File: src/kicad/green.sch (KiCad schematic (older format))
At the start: 0 parts

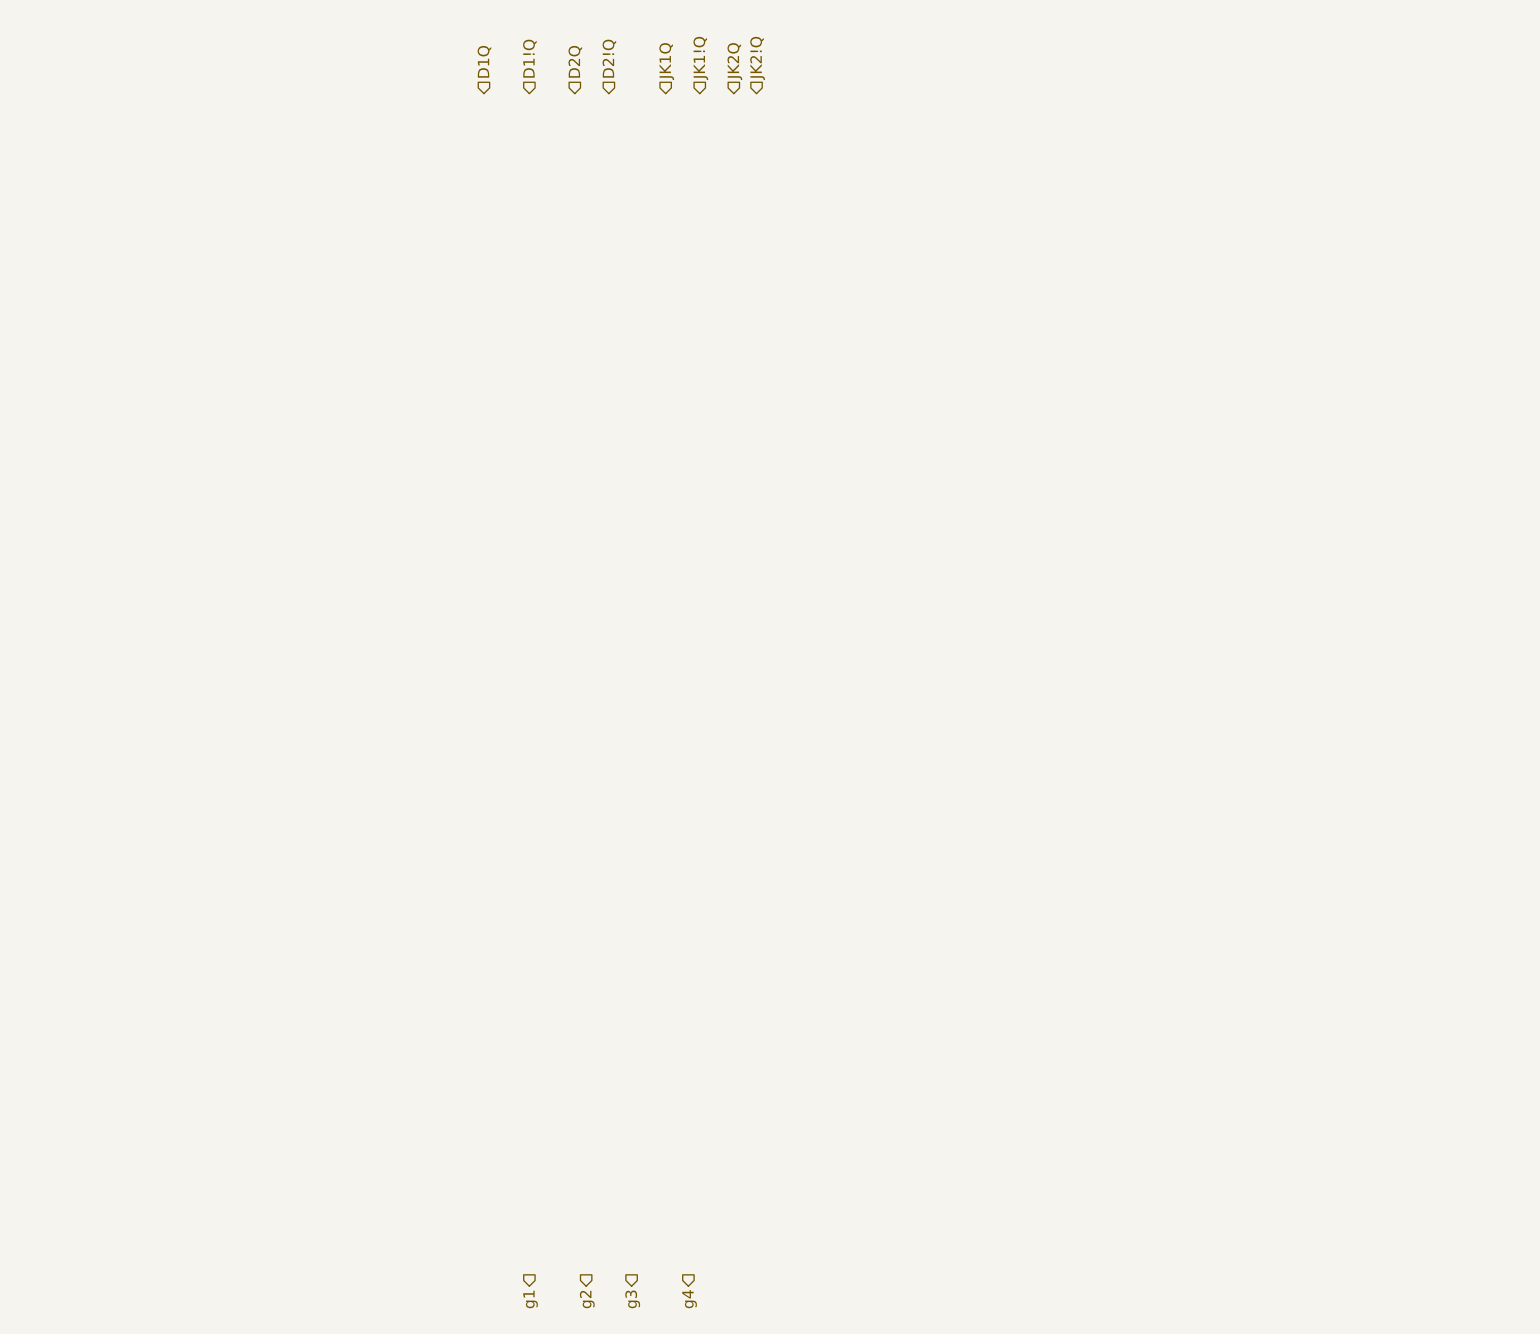
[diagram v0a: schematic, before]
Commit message: finished sub-schemes for LEDs
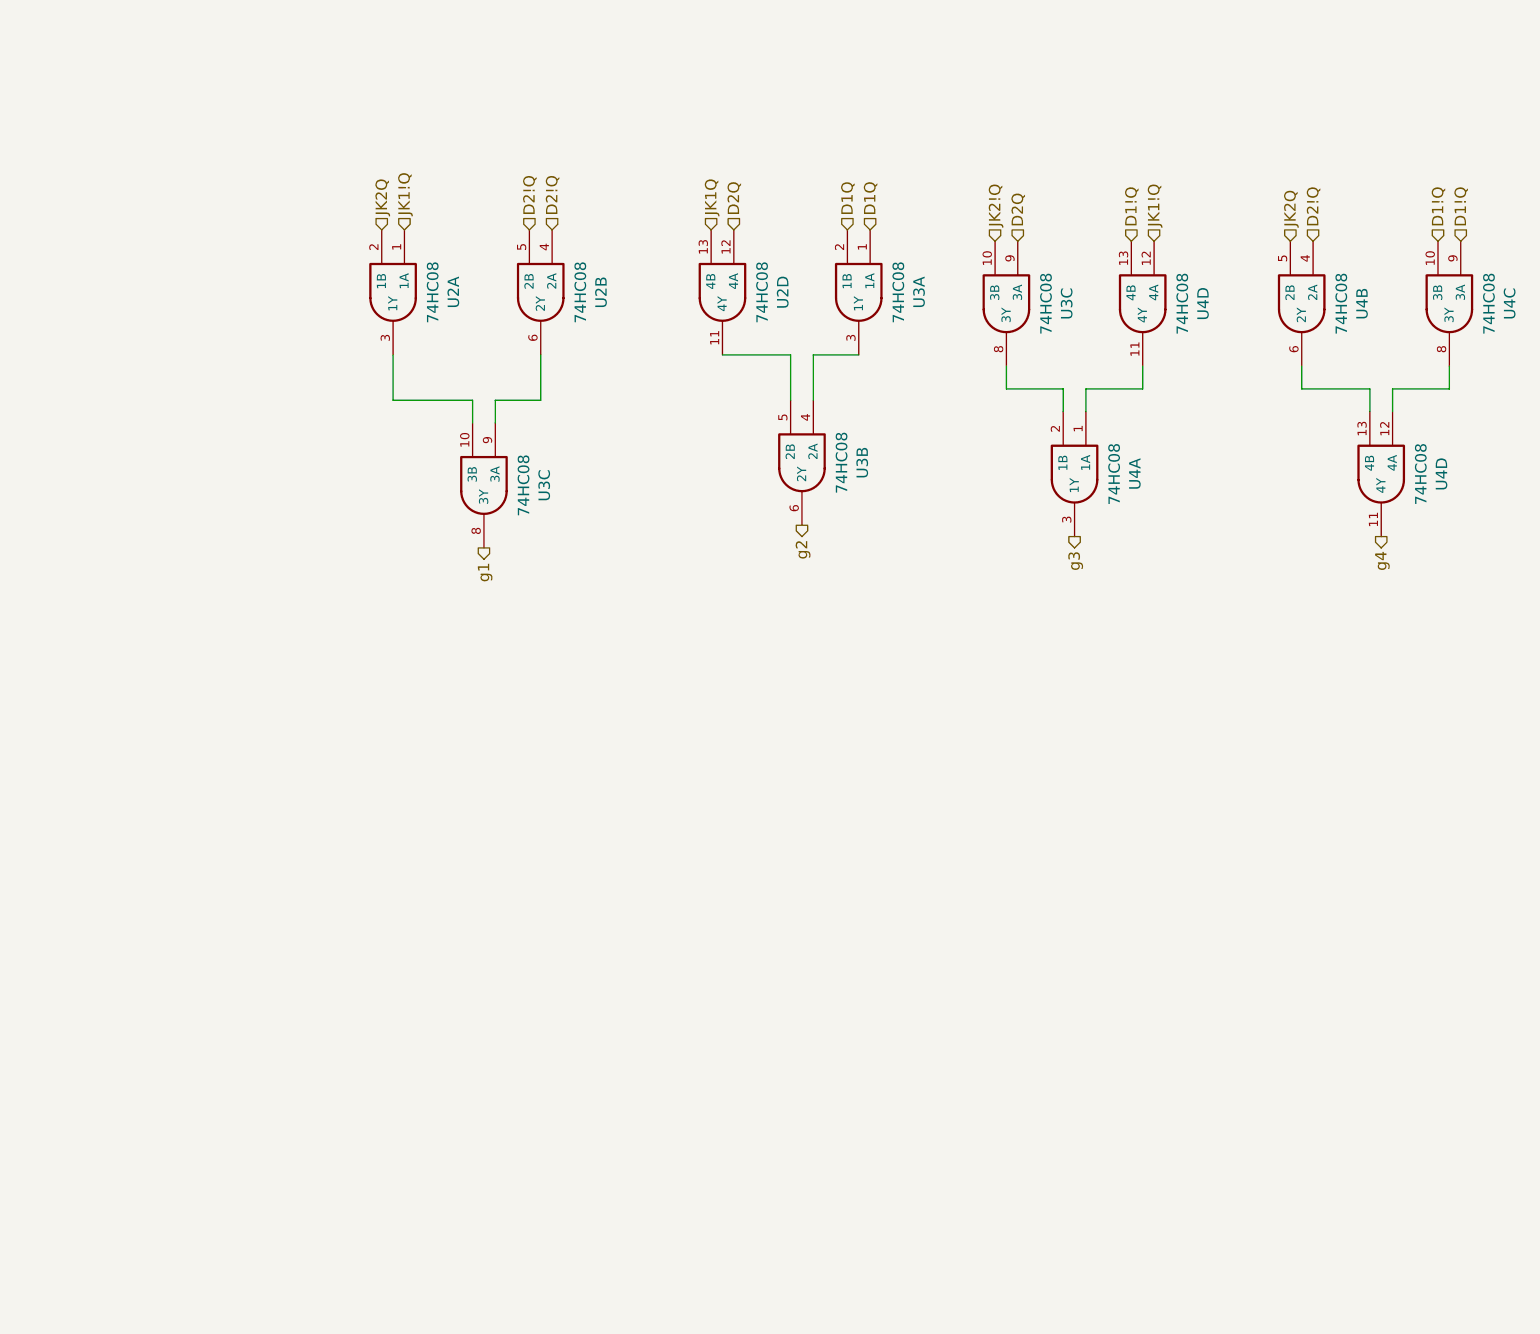
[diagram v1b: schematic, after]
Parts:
- added U2, U3 (x2), U4 (x2): 74HC08, Housings_SOIC:SOIC-14_3.9x8.7mm_Pitch1.27mm, symbol PB170:74HC08
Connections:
- net D1!Q: now also U4.10 (3B), U4.13 (4B), U4.9 (3A)
- net D1Q: now also U3.1 (1A), U3.2 (1B)
- net D2!Q: now also U2.4 (2A), U2.5 (2B), U4.4 (2A)
- net D2Q: now also U2.12 (4A), U3.9 (3A)
- net JK1!Q: now also U2.1 (1A), U4.12 (4A)
- net JK1Q: now also U2.13 (4B)
- net JK2!Q: now also U3.10 (3B)
- net JK2Q: now also U2.2 (1B), U4.5 (2B)
- net g1: now also U3.8 (3Y)
- net g2: now also U3.6 (2Y)
- net g3: now also U4.3 (1Y)
- net g4: now also U4.11 (4Y)
- new net: U2.3 (1Y), U3.10 (3B)
- new net: U2.6 (2Y), U3.9 (3A)
- new net: U2.11 (4Y), U3.5 (2B)
- new net: U3.3 (1Y), U3.4 (2A)
- new net: U3.8 (3Y), U4.2 (1B)
- new net: U4.1 (1A), U4.11 (4Y)
- new net: U4.13 (4B), U4.6 (2Y)
- new net: U4.12 (4A), U4.8 (3Y)

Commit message: fixed annotaion
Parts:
- renumbered U3 to U2, U4 to U3
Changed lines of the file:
@@
 $Descr A4 11693 8268
 encoding utf-8
-Sheet 5 6
+Sheet 4 5
 Title ""
 Date ""
@@
 P 2800 3200
 AR Path="/5FFE1BA5" Ref="U?"  Part="2"
-AR Path="/6006FC3B/5FFE1BA5" Ref="U3"  Part="3"
-F 0 "U3" H 2825 3467 50  0000 C CNN
+AR Path="/6006FC3B/5FFE1BA5" Ref="U2"  Part="3"
+F 0 "U2" H 2825 3467 50  0000 C CNN
 F 1 "74HC08" H 2825 3376 50  0000 C CNN
 F 2 "Housings_SOIC:SOIC-14_3.9x8.7mm_Pitch1.27mm" H 2800 3200 50  0001 C CNN
@@
 P 6750 3150
 AR Path="/5FFEBE04" Ref="U?"  Part="2"
-AR Path="/6006FC3B/5FFEBE04" Ref="U4"  Part="4"
-F 0 "U4" H 6775 3417 50  0000 C CNN
+AR Path="/6006FC3B/5FFEBE04" Ref="U3"  Part="4"
+F 0 "U3" H 6775 3417 50  0000 C CNN
 F 1 "74HC08" H 6775 3326 50  0000 C CNN
 F 2 "Housings_SOIC:SOIC-14_3.9x8.7mm_Pitch1.27mm" H 6750 3150 50  0001 C CNN

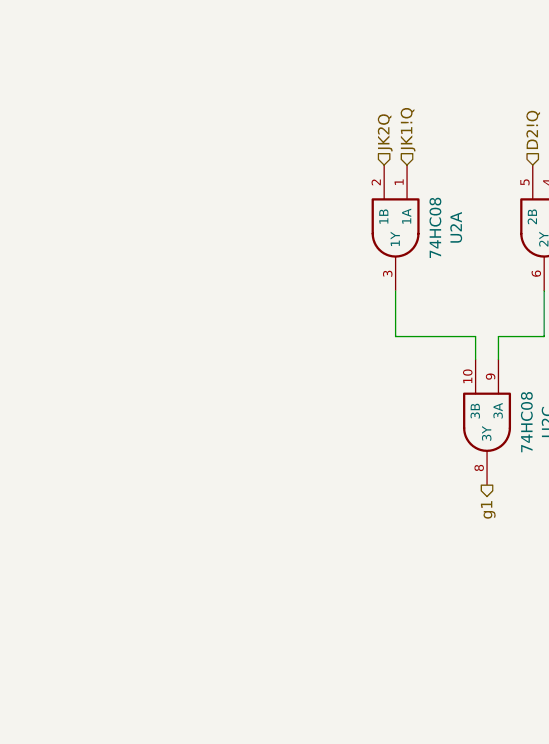
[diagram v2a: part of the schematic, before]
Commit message: added annotations, power connections to parts
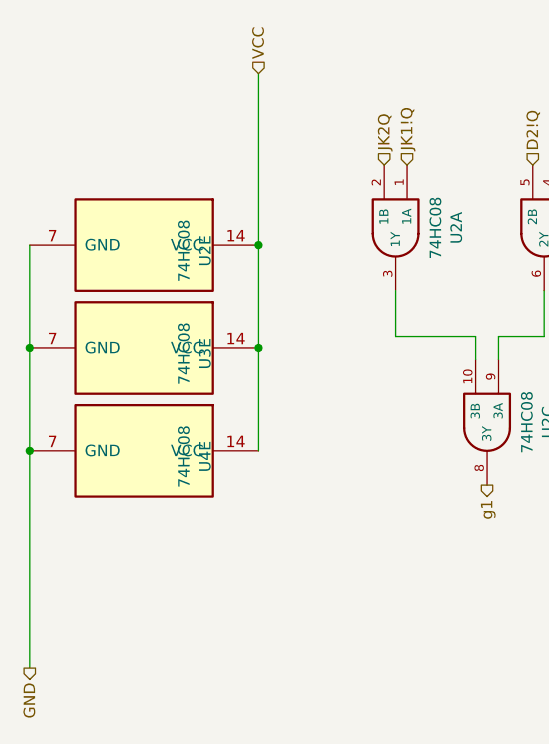
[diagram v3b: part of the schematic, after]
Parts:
- added unit 5 of U2
- added unit 5 of U3
- added unit 5 of U4
- U2, U3, U4: footprint Housings_SOIC:SOIC-14_3.9x8.7mm_Pitch1.27mm -> Package_SO:SOIC-14_3.9x8.7mm_P1.27mm
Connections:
- new net GND: U2.7 (GND), U3.7 (GND), U4.7 (GND)
- new net VCC: U2.14 (VCC), U3.14 (VCC), U4.14 (VCC)
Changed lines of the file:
@@
 F 0 "U2" H 2425 2617 50  0000 C CNN
 F 1 "74HC08" H 2425 2526 50  0000 C CNN
-F 2 "Housings_SOIC:SOIC-14_3.9x8.7mm_Pitch1.27mm" H 2400 2350 50  0001 C CNN
+F 2 "Package_SO:SOIC-14_3.9x8.7mm_P1.27mm" H 2400 2350 50  0001 C CNN
 F 3 "https://datasheet.lcsc.com/szlcsc/Nexperia-74HC08D-653_C5593.pdf" H 2400 2350 50  0001 C CNN
 F 4 "C5593" H 2400 2350 50  0001 C CNN "LCSC"
@@
 F 0 "U2" H 3075 2617 50  0000 C CNN
 F 1 "74HC08" H 3075 2526 50  0000 C CNN
-F 2 "Housings_SOIC:SOIC-14_3.9x8.7mm_Pitch1.27mm" H 3050 2350 50  0001 C CNN
+F 2 "Package_SO:SOIC-14_3.9x8.7mm_P1.27mm" H 3050 2350 50  0001 C CNN
 F 3 "https://datasheet.lcsc.com/szlcsc/Nexperia-74HC08D-653_C5593.pdf" H 3050 2350 50  0001 C CNN
 F 4 "C5593" H 3050 2350 50  0001 C CNN "LCSC"
@@
 F 0 "U2" H 2825 3467 50  0000 C CNN
 F 1 "74HC08" H 2825 3376 50  0000 C CNN
-F 2 "Housings_SOIC:SOIC-14_3.9x8.7mm_Pitch1.27mm" H 2800 3200 50  0001 C CNN
+F 2 "Package_SO:SOIC-14_3.9x8.7mm_P1.27mm" H 2800 3200 50  0001 C CNN
 F 3 "https://datasheet.lcsc.com/szlcsc/Nexperia-74HC08D-653_C5593.pdf" H 2800 3200 50  0001 C CNN
 F 4 "C5593" H 2800 3200 50  0001 C CNN "LCSC"
@@
 F 0 "U2" H 3875 2617 50  0000 C CNN
 F 1 "74HC08" H 3875 2526 50  0000 C CNN
-F 2 "Housings_SOIC:SOIC-14_3.9x8.7mm_Pitch1.27mm" H 3850 2350 50  0001 C CNN
+F 2 "Package_SO:SOIC-14_3.9x8.7mm_P1.27mm" H 3850 2350 50  0001 C CNN
 F 3 "https://datasheet.lcsc.com/szlcsc/Nexperia-74HC08D-653_C5593.pdf" H 3850 2350 50  0001 C CNN
 F 4 "C5593" H 3850 2350 50  0001 C CNN "LCSC"
@@
 F 0 "U3" H 4475 2617 50  0000 C CNN
 F 1 "74HC08" H 4475 2526 50  0000 C CNN
-F 2 "Housings_SOIC:SOIC-14_3.9x8.7mm_Pitch1.27mm" H 4450 2350 50  0001 C CNN
+F 2 "Package_SO:SOIC-14_3.9x8.7mm_P1.27mm" H 4450 2350 50  0001 C CNN
 F 3 "https://datasheet.lcsc.com/szlcsc/Nexperia-74HC08D-653_C5593.pdf" H 4450 2350 50  0001 C CNN
 F 4 "C5593" H 4450 2350 50  0001 C CNN "LCSC"
@@
 F 0 "U3" H 4225 3367 50  0000 C CNN
 F 1 "74HC08" H 4225 3276 50  0000 C CNN
-F 2 "Housings_SOIC:SOIC-14_3.9x8.7mm_Pitch1.27mm" H 4200 3100 50  0001 C CNN
+F 2 "Package_SO:SOIC-14_3.9x8.7mm_P1.27mm" H 4200 3100 50  0001 C CNN
 F 3 "https://datasheet.lcsc.com/szlcsc/Nexperia-74HC08D-653_C5593.pdf" H 4200 3100 50  0001 C CNN
 F 4 "C5593" H 4200 3100 50  0001 C CNN "LCSC"
@@
 F 0 "U3" H 5125 2667 50  0000 C CNN
 F 1 "74HC08" H 5125 2576 50  0000 C CNN
-F 2 "Housings_SOIC:SOIC-14_3.9x8.7mm_Pitch1.27mm" H 5100 2400 50  0001 C CNN
+F 2 "Package_SO:SOIC-14_3.9x8.7mm_P1.27mm" H 5100 2400 50  0001 C CNN
 F 3 "https://datasheet.lcsc.com/szlcsc/Nexperia-74HC08D-653_C5593.pdf" H 5100 2400 50  0001 C CNN
 F 4 "C5593" H 5100 2400 50  0001 C CNN "LCSC"
@@
 F 0 "U4" H 5725 2667 50  0000 C CNN
 F 1 "74HC08" H 5725 2576 50  0000 C CNN
-F 2 "Housings_SOIC:SOIC-14_3.9x8.7mm_Pitch1.27mm" H 5700 2400 50  0001 C CNN
+F 2 "Package_SO:SOIC-14_3.9x8.7mm_P1.27mm" H 5700 2400 50  0001 C CNN
 F 3 "https://datasheet.lcsc.com/szlcsc/Nexperia-74HC08D-653_C5593.pdf" H 5700 2400 50  0001 C CNN
 F 4 "C5593" H 5700 2400 50  0001 C CNN "LCSC"
@@
 F 0 "U4" H 5425 3417 50  0000 C CNN
 F 1 "74HC08" H 5425 3326 50  0000 C CNN
-F 2 "Housings_SOIC:SOIC-14_3.9x8.7mm_Pitch1.27mm" H 5400 3150 50  0001 C CNN
+F 2 "Package_SO:SOIC-14_3.9x8.7mm_P1.27mm" H 5400 3150 50  0001 C CNN
 F 3 "https://datasheet.lcsc.com/szlcsc/Nexperia-74HC08D-653_C5593.pdf" H 5400 3150 50  0001 C CNN
 F 4 "C5593" H 5400 3150 50  0001 C CNN "LCSC"
@@
 F 0 "U4" H 6425 2667 50  0000 C CNN
 F 1 "74HC08" H 6425 2576 50  0000 C CNN
-F 2 "Housings_SOIC:SOIC-14_3.9x8.7mm_Pitch1.27mm" H 6400 2400 50  0001 C CNN
+F 2 "Package_SO:SOIC-14_3.9x8.7mm_P1.27mm" H 6400 2400 50  0001 C CNN
 F 3 "https://datasheet.lcsc.com/szlcsc/Nexperia-74HC08D-653_C5593.pdf" H 6400 2400 50  0001 C CNN
 F 4 "C5593" H 6400 2400 50  0001 C CNN "LCSC"
@@
 F 0 "U4" H 7075 2667 50  0000 C CNN
 F 1 "74HC08" H 7075 2576 50  0000 C CNN
-F 2 "Housings_SOIC:SOIC-14_3.9x8.7mm_Pitch1.27mm" H 7050 2400 50  0001 C CNN
+F 2 "Package_SO:SOIC-14_3.9x8.7mm_P1.27mm" H 7050 2400 50  0001 C CNN
 F 3 "https://datasheet.lcsc.com/szlcsc/Nexperia-74HC08D-653_C5593.pdf" H 7050 2400 50  0001 C CNN
 F 4 "C5593" H 7050 2400 50  0001 C CNN "LCSC"
@@
 F 0 "U3" H 6775 3417 50  0000 C CNN
 F 1 "74HC08" H 6775 3326 50  0000 C CNN
-F 2 "Housings_SOIC:SOIC-14_3.9x8.7mm_Pitch1.27mm" H 6750 3150 50  0001 C CNN
+F 2 "Package_SO:SOIC-14_3.9x8.7mm_P1.27mm" H 6750 3150 50  0001 C CNN
 F 3 "https://datasheet.lcsc.com/szlcsc/Nexperia-74HC08D-653_C5593.pdf" H 6750 3150 50  0001 C CNN
 F 4 "C5593" H 6750 3150 50  0001 C CNN "LCSC"
@@
 Text HLabel 7100 2150 1    50   Input ~ 0
 D1!Q
+$Comp
+L PB170:74HC08 U?
+U 5 1 606691F5
+P 1300 2450
+AR Path="/606691F5" Ref="U?"  Part="2"
+AR Path="/6006FC3B/606691F5" Ref="U2"  Part="5"
+AR Path="/6004480C/606691F5" Ref="U?"  Part="5"
+F 0 "U2" H 1325 2717 50  0000 C CNN
+F 1 "74HC08" H 1325 2626 50  0000 C CNN
+F 2 "Package_SO:SOIC-14_3.9x8.7mm_P1.27mm" H 1300 2450 50  0001 C CNN
+F 3 "https://datasheet.lcsc.com/szlcsc/Nexperia-74HC08D-653_C5593.pdf" H 1300 2450 50  0001 C CNN
+F 4 "C5593" H 1300 2450 50  0001 C CNN "LCSC"
+	5    1300 2450
+	0    1    1    0
+$EndComp
+$Comp
+L PB170:74HC08 U?
+U 5 1 606698AA
+P 1300 2900
+AR Path="/606698AA" Ref="U?"  Part="2"
+AR Path="/6006FC3B/606698AA" Ref="U3"  Part="5"
+AR Path="/6004480C/606698AA" Ref="U?"  Part="5"
+F 0 "U3" H 1325 3167 50  0000 C CNN
+F 1 "74HC08" H 1325 3076 50  0000 C CNN
+F 2 "Package_SO:SOIC-14_3.9x8.7mm_P1.27mm" H 1300 2900 50  0001 C CNN
+F 3 "https://datasheet.lcsc.com/szlcsc/Nexperia-74HC08D-653_C5593.pdf" H 1300 2900 50  0001 C CNN
+F 4 "C5593" H 1300 2900 50  0001 C CNN "LCSC"
+	5    1300 2900
+	0    1    1    0
+$EndComp
+$Comp
+L PB170:74HC08 U?
+U 5 1 60669DC5
+P 1300 3350
+AR Path="/60669DC5" Ref="U?"  Part="2"
+AR Path="/6006FC3B/60669DC5" Ref="U4"  Part="5"
+AR Path="/6004480C/60669DC5" Ref="U?"  Part="5"
+F 0 "U4" H 1325 3617 50  0000 C CNN
+F 1 "74HC08" H 1325 3526 50  0000 C CNN
+F 2 "Package_SO:SOIC-14_3.9x8.7mm_P1.27mm" H 1300 3350 50  0001 C CNN
+F 3 "https://datasheet.lcsc.com/szlcsc/Nexperia-74HC08D-653_C5593.pdf" H 1300 3350 50  0001 C CNN
+F 4 "C5593" H 1300 3350 50  0001 C CNN "LCSC"
+	5    1300 3350
+	0    1    1    0
+$EndComp
+Wire Wire Line
+	800  2900 800  2450
+Wire Wire Line
+	800  2900 800  3350
+Connection ~ 800  2900
+Connection ~ 800  3350
+Wire Wire Line
+	800  3350 800  4300
+Wire Wire Line
+	1800 3350 1800 2900
+Wire Wire Line
+	1800 2900 1800 2450
+Connection ~ 1800 2900
+Wire Wire Line
+	1800 2450 1800 1700
+Connection ~ 1800 2450
+Text HLabel 1800 1700 1    50   Input ~ 0
+VCC
+Text HLabel 800  4300 3    50   Output ~ 0
+GND
 $EndSCHEMATC

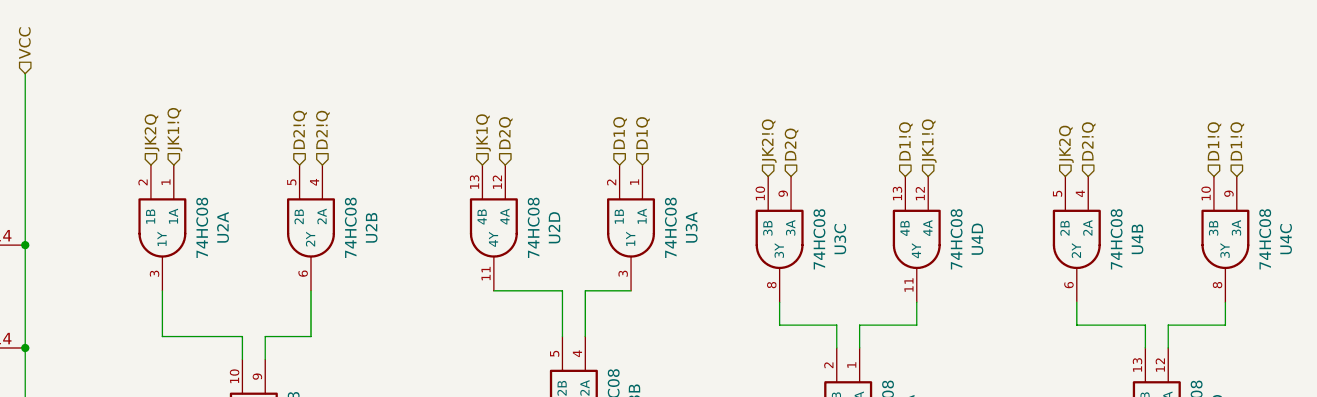
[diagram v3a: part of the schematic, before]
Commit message: Corrected negations
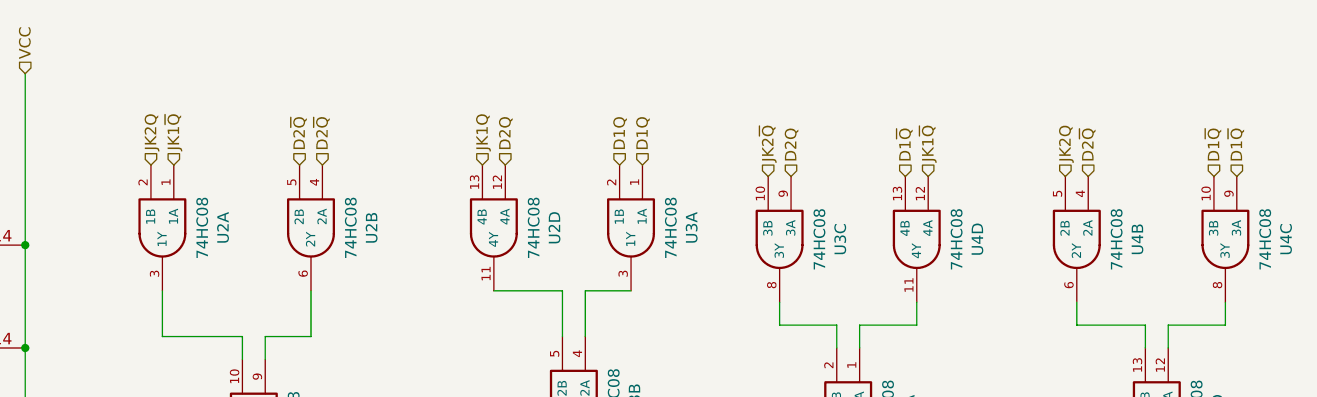
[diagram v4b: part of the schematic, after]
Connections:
- net D1!Q renamed D1~Q
- net D2!Q renamed D2~Q
- net JK1!Q renamed JK1~Q
- net JK2!Q renamed JK2~Q
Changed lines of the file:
@@
 D1Q
 Text HLabel 5650 2150 1    50   Input ~ 0
-D1!Q
+D1~Q
 Text HLabel 3900 2100 1    50   Input ~ 0
 D2Q
 Text HLabel 3000 2100 1    50   Input ~ 0
-D2!Q
+D2~Q
 Text HLabel 3800 2100 1    50   Input ~ 0
 JK1Q
 Text HLabel 2450 2100 1    50   Input ~ 0
-JK1!Q
+JK1~Q
 Text HLabel 2350 2100 1    50   Input ~ 0
 JK2Q
-Text HLabel 5050 2150 1    50   Input ~ 0
-JK2!Q
 Text HLabel 2800 3500 3    50   Output ~ 0
 g1
@@
 	2850 2850 2850 2950
 Text HLabel 3100 2100 1    50   Input ~ 0
-D2!Q
+D2~Q
 $Comp
 L PB170:74HC08 U?
@@
 D2Q
 Text HLabel 5750 2150 1    50   Input ~ 0
-JK1!Q
+JK1~Q
 $Comp
 L PB170:74HC08 U?
@@
 JK2Q
 Text HLabel 6450 2150 1    50   Input ~ 0
-D2!Q
+D2~Q
 Text HLabel 7000 2150 1    50   Input ~ 0
-D1!Q
+D1~Q
 Text HLabel 7100 2150 1    50   Input ~ 0
-D1!Q
+D1~Q
 $Comp
 L PB170:74HC08 U?
@@
 Text HLabel 800  4300 3    50   Output ~ 0
 GND
+Text HLabel 5050 2150 1    50   Input ~ 0
+JK2~Q
 $EndSCHEMATC
